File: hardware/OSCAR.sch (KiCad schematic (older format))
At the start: 0 parts

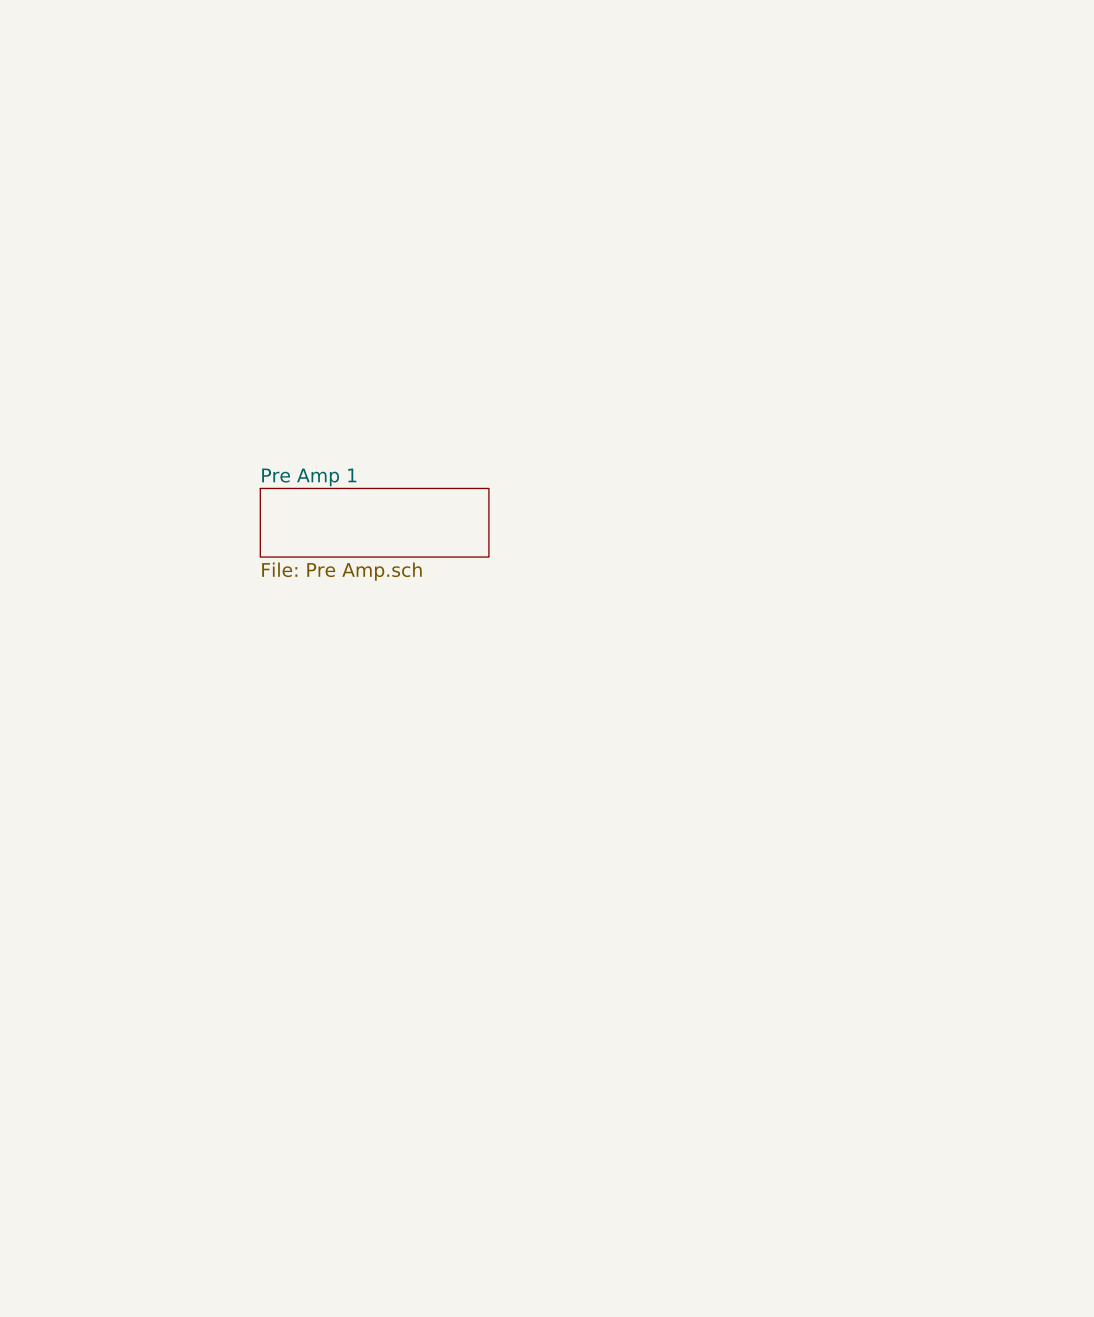
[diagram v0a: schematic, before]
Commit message: Added PCM 4204 and wired to pre amps
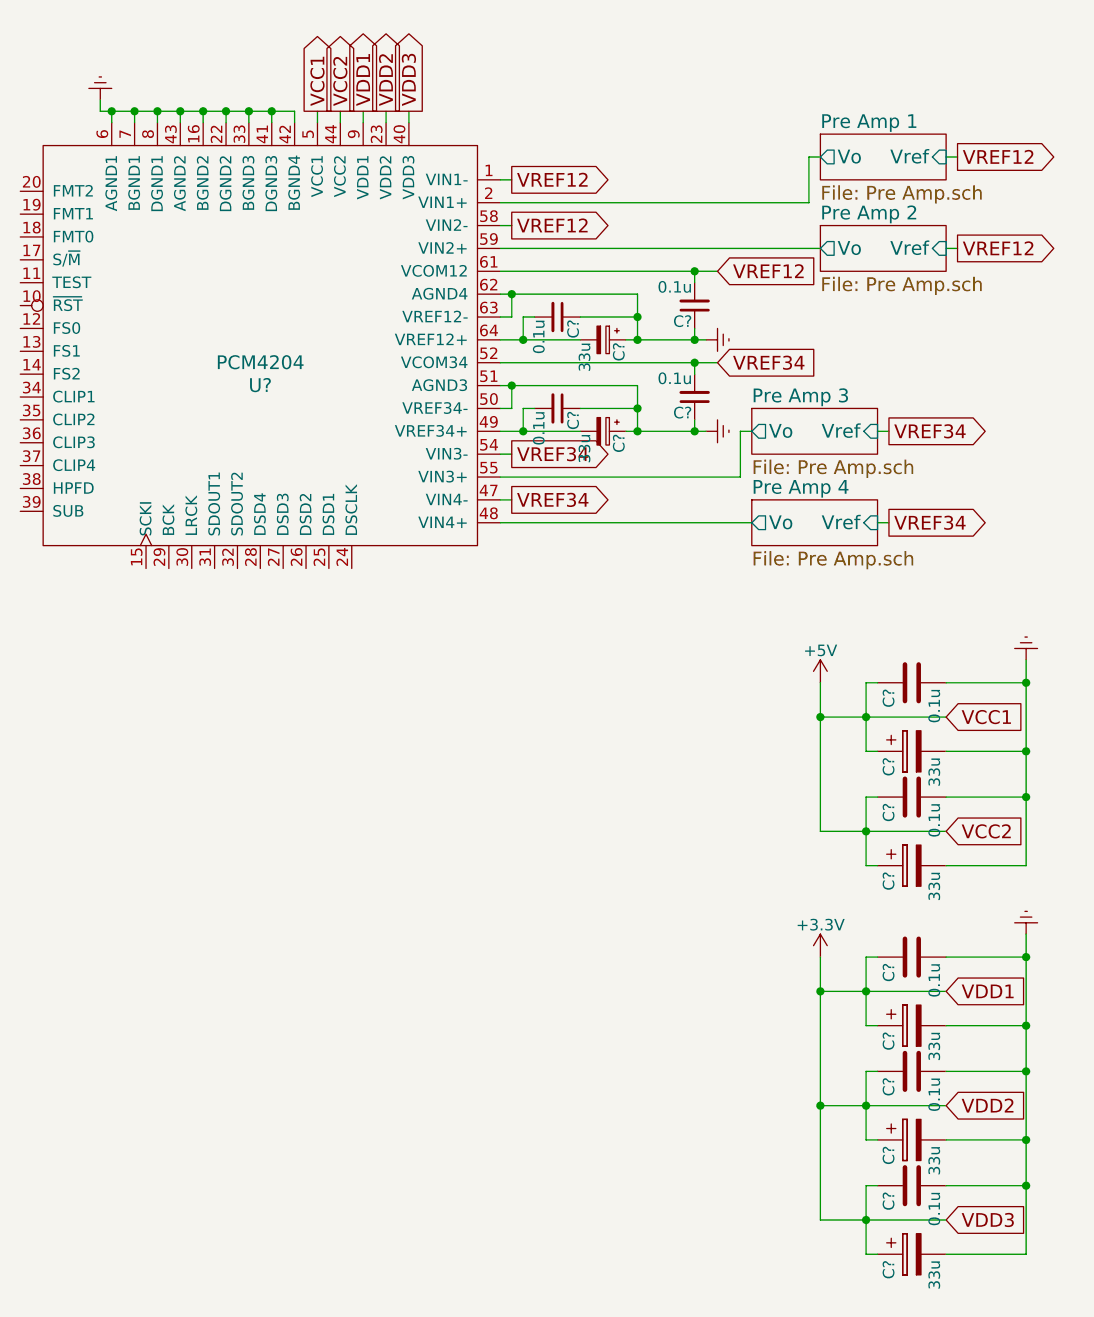
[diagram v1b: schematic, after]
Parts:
- added C? (x5): 0.1u, symbol C
- added C? (x5): 33u, symbol CP
- added C? (x4): 0.1u, symbol C_Small
- added C? (x2): 33u, symbol CP_Small
- added U?: PCM4204, symbol PCM4204
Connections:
- new net: C?.2, C?.2, U?.49 (VREF34+)
- new net: C?.2, C?.2, U?.64 (VREF12+)
- new net +3V3: C?.1, C?.1, C?.1, C?.1, C?.1, C?.1, U?.23 (VDD2), U?.40 (VDD3), U?.9 (VDD1)
- new net +5V: C?.1, C?.1, C?.1, C?.1, U?.44 (VCC2), U?.5 (VCC1)
- new net Earth: C?.1, C?.1, C?.1, C?.1, C?.1, C?.1, C?.2, C?.2, C?.2, C?.2, C?.2, C?.2, C?.2, C?.2, C?.2, C?.2, U?.16 (BGND2), U?.22 (DGND2), U?.33 (BGND3), U?.41 (DGND3), U?.42 (BGND4), U?.43 (AGND2), U?.50 (VREF34-), U?.51 (AGND3), U?.6 (AGND1), U?.62 (AGND4), U?.63 (VREF12-), U?.7 (BGND1), U?.8 (DGND1)
- new net Pre Amp 1/Vo: U?.2 (VIN1+)
- new net Pre Amp 2/Vo: U?.59 (VIN2+)
- new net Pre Amp 3/Vo: U?.55 (VIN3+)
- new net Pre Amp 4/Vo: U?.48 (VIN4+)
- new net VREF12: C?.2, U?.1 (VIN1-), U?.58 (VIN2-), U?.61 (VCOM12)
- new net VREF34: C?.2, U?.47 (VIN4-), U?.52 (VCOM34), U?.54 (VIN3-)

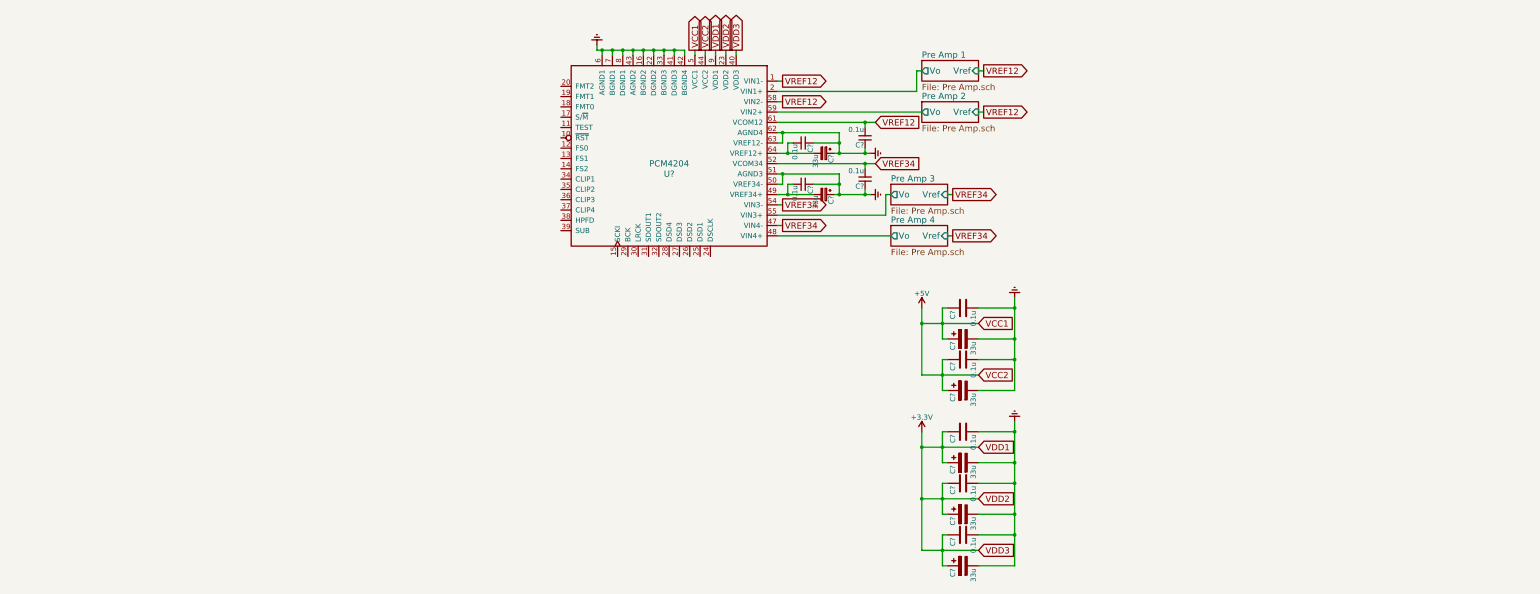
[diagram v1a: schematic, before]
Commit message: Add STM32 to Schematic
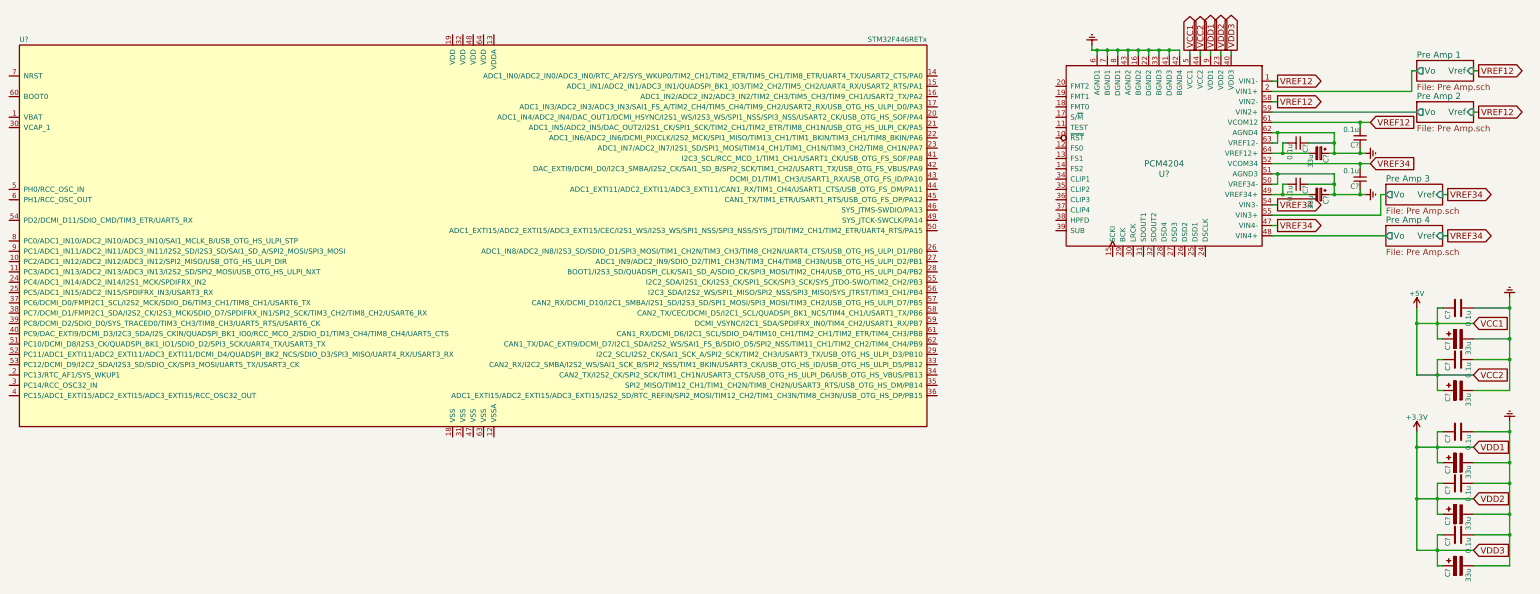
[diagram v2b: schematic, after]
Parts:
- added U?: STM32F446RETx, LQFP64, symbol STM32F446RETx
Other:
- moved on the sheet: C?, U?

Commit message: Added I2S connections and pin flags
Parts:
- added J?: USB_B, symbol USB_B
- added R? (x5): 100, symbol R
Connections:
- net +5V: now also J?.1 (VBUS)
- net Earth: now also U?.11 (TEST), J?.4 (GND), J?.5 (Shield)
- net RST: now reaches U?.10 (~RST)
- net FS0: now reaches U?.12 (FS0)
- net FS1: now reaches U?.13 (FS1)
- net FS2: now reaches U?.14 (FS2)
- net at U?.15 (SCKI): now also R?.1
- net S/~M: now reaches U?.17 (S/~M)
- net FMT0: now reaches U?.18 (FMT0)
- net FMT1: now reaches U?.19 (FMT1)
- net FMT2: now reaches U?.20 (FMT2)
- net at U?.29 (BCK): now also R?.1
- net at U?.30 (LRCK): now also R?.1
- net at U?.31 (SDOUT1): now also R?.1
- net at U?.32 (SDOUT2): now also R?.1
- net CLIP1: now reaches U?.34 (CLIP1)
- net CLIP2: now reaches U?.35 (CLIP2)
- net CLIP3: now reaches U?.36 (CLIP3)
- net CLIP4: now reaches U?.37 (CLIP4)
- net HPDF: now reaches U?.38 (HPFD)
- net SUB: now reaches U?.39 (SUB)
- net SCKI: now reaches U?.24 (PC4/ADC1_IN14/ADC2_IN14/I2S1_MCK/SPDIFRX_IN2)
- net SCKI: now also R?.2
- net BCK: now reaches U?.34 (CAN2_TX/I2S2_CK/SPI2_SCK/TIM1_CH1N/USART3_CTS/USB_OTG_HS_ULPI_D6/USB_OTG_HS_VBUS/PB13)
- net BCK: now also U?.55 (I2C2_SDA/I2S1_CK/I2S3_CK/SPI1_SCK/SPI3_SCK/SYS_JTDO-SWO/TIM2_CH2/PB3), R?.2
- net SD2: now reaches U?.36 (ADC1_EXTI15/ADC2_EXTI15/ADC3_EXTI15/I2S2_SD/RTC_REFIN/SPI2_MOSI/TIM12_CH2/TIM1_CH3N/TIM8_CH3N/USB_OTG_HS_DP/PB15)
- net SD2: now also R?.2
- net LRCK: now reaches U?.56 (I2C3_SDA/I2S2_WS/SPI1_MISO/SPI2_NSS/SPI3_MISO/SYS_JTRST/TIM3_CH1/PB4)
- net LRCK: now also R?.2
- net SD1: now reaches U?.57 (CAN2_RX/DCMI_D10/I2C1_SMBA/I2S1_SD/I2S3_SD/SPI1_MOSI/SPI3_MOSI/TIM3_CH2/USB_OTG_HS_ULPI_D7/PB5)
- net SD1: now also R?.2
- no-connect marks 0 -> 5
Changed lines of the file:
@@
 $EndComp
 $Comp
-L Earth #PWR?
+L Earth #PWR01
 U 1 1 595B8693
 P 11800 800
-F 0 "#PWR?" H 11800 550 50  0001 C CNN
+F 0 "#PWR01" H 11800 550 50  0001 C CNN
 F 1 "Earth" H 11800 650 50  0001 C CNN
 F 2 "" H 11800 800 50  0001 C CNN
@@
 VDD3
 $Comp
-L +5V #PWR?
+L +5V #PWR02
 U 1 1 595B9388
 P 14950 3350
-F 0 "#PWR?" H 14950 3200 50  0001 C CNN
+F 0 "#PWR02" H 14950 3200 50  0001 C CNN
 F 1 "+5V" H 14950 3490 50  0000 C CNN
 F 2 "" H 14950 3350 50  0001 C CNN
@@
 $EndComp
 $Comp
-L Earth #PWR?
+L Earth #PWR03
 U 1 1 595B9522
 P 15850 3250
-F 0 "#PWR?" H 15850 3000 50  0001 C CNN
+F 0 "#PWR03" H 15850 3000 50  0001 C CNN
 F 1 "Earth" H 15850 3100 50  0001 C CNN
 F 2 "" H 15850 3250 50  0001 C CNN
@@
 $EndComp
 $Comp
-L Earth #PWR?
+L Earth #PWR04
 U 1 1 595B9A44
 P 15850 4450
-F 0 "#PWR?" H 15850 4200 50  0001 C CNN
+F 0 "#PWR04" H 15850 4200 50  0001 C CNN
 F 1 "Earth" H 15850 4300 50  0001 C CNN
 F 2 "" H 15850 4450 50  0001 C CNN
@@
 Connection ~ 15850 3850
 $Comp
-L +3.3V #PWR?
+L +3.3V #PWR05
 U 1 1 595B9EEC
 P 14950 4550
-F 0 "#PWR?" H 14950 4400 50  0001 C CNN
+F 0 "#PWR05" H 14950 4400 50  0001 C CNN
 F 1 "+3.3V" H 14950 4690 50  0000 C CNN
 F 2 "" H 14950 4550 50  0001 C CNN
@@
 Connection ~ 13650 1850
 $Comp
-L Earth #PWR?
+L Earth #PWR06
 U 1 1 595BB36D
 P 14450 1850
-F 0 "#PWR?" H 14450 1600 50  0001 C CNN
+F 0 "#PWR06" H 14450 1600 50  0001 C CNN
 F 1 "Earth" H 14450 1700 50  0001 C CNN
 F 2 "" H 14450 1850 50  0001 C CNN
@@
 Connection ~ 13650 2250
 $Comp
-L Earth #PWR?
+L Earth #PWR07
 U 1 1 595BBE98
 P 14450 2250
-F 0 "#PWR?" H 14450 2000 50  0001 C CNN
+F 0 "#PWR07" H 14450 2000 50  0001 C CNN
 F 1 "Earth" H 14450 2100 50  0001 C CNN
 F 2 "" H 14450 2250 50  0001 C CNN
@@
 Text GLabel 13600 1350 2    60   Output ~ 0
 VREF12
-Text GLabel 13600 2350 2    60   Output ~ 0
+Text GLabel 14100 2350 2    60   Output ~ 0
 VREF34
 Text GLabel 13600 2550 2    60   Output ~ 0
@@
 	13550 1150 13600 1150
 Wire Wire Line
-	13550 2350 13600 2350
+	13550 2350 14100 2350
 Wire Wire Line
 	13550 2550 13600 2550
@@
 	1    0    0    -1
 $EndComp
+Text GLabel 12000 3150 3    60   Output ~ 0
+SCKI
+Text GLabel 12100 3150 3    60   BiDi ~ 0
+BCK
+Text GLabel 12200 3150 3    60   BiDi ~ 0
+LRCK
+Text GLabel 12300 3150 3    60   Input ~ 0
+SD1
+Text GLabel 12400 3150 3    60   Input ~ 0
+SD2
+$Comp
+L R R?
+U 1 1 595C4B9A
+P 12000 3000
+F 0 "R?" V 12080 3000 50  0000 C CNN
+F 1 "100" V 12000 3000 50  0000 C CNN
+F 2 "" V 11930 3000 50  0001 C CNN
+F 3 "" H 12000 3000 50  0001 C CNN
+	1    12000 3000
+	1    0    0    -1
+$EndComp
+$Comp
+L R R?
+U 1 1 595C4DB7
+P 12100 3000
+F 0 "R?" V 12180 3000 50  0000 C CNN
+F 1 "100" V 12100 3000 50  0000 C CNN
+F 2 "" V 12030 3000 50  0001 C CNN
+F 3 "" H 12100 3000 50  0001 C CNN
+	1    12100 3000
+	1    0    0    -1
+$EndComp
+$Comp
+L R R?
+U 1 1 595C4EC7
+P 12200 3000
+F 0 "R?" V 12280 3000 50  0000 C CNN
+F 1 "100" V 12200 3000 50  0000 C CNN
+F 2 "" V 12130 3000 50  0001 C CNN
+F 3 "" H 12200 3000 50  0001 C CNN
+	1    12200 3000
+	1    0    0    -1
+$EndComp
+$Comp
+L R R?
+U 1 1 595C4ECD
+P 12300 3000
+F 0 "R?" V 12380 3000 50  0000 C CNN
+F 1 "100" V 12300 3000 50  0000 C CNN
+F 2 "" V 12230 3000 50  0001 C CNN
+F 3 "" H 12300 3000 50  0001 C CNN
+	1    12300 3000
+	1    0    0    -1
+$EndComp
+$Comp
+L R R?
+U 1 1 595C4F19
+P 12400 3000
+F 0 "R?" V 12480 3000 50  0000 C CNN
+F 1 "100" V 12400 3000 50  0000 C CNN
+F 2 "" V 12330 3000 50  0001 C CNN
+F 3 "" H 12400 3000 50  0001 C CNN
+	1    12400 3000
+	1    0    0    -1
+$EndComp
+Text GLabel 10350 3100 2    60   BiDi ~ 0
+BCK
+Text GLabel 10350 3200 2    60   BiDi ~ 0
+LRCK
+Text GLabel 10350 3300 2    60   Output ~ 0
+SD1
+Text GLabel 10350 4200 2    60   Output ~ 0
+SD2
+Text GLabel 10350 4000 2    60   BiDi ~ 0
+BCK
+Wire Wire Line
+	10300 3100 10350 3100
+Wire Wire Line
+	10300 3200 10350 3200
+Wire Wire Line
+	10300 3300 10350 3300
+Wire Wire Line
+	10300 4000 10350 4000
+Wire Wire Line
+	10300 4200 10350 4200
+Text GLabel 1250 3100 0    60   Input ~ 0
+SCKI
+Wire Wire Line
+	1250 3100 1300 3100
+$Comp
+L USB_B J?
+U 1 1 595C8EF7
+P 1700 9700
+F 0 "J?" H 1500 10150 50  0000 L CNN
+F 1 "USB_B" H 1500 10050 50  0000 L CNN
+F 2 "" H 1850 9650 50  0001 C CNN
+F 3 "" H 1850 9650 50  0001 C CNN
+	1    1700 9700
+	1    0    0    -1
+$EndComp
+$Comp
+L +5V #PWR08
+U 1 1 595C96F2
+P 2050 9500
+F 0 "#PWR08" H 2050 9350 50  0001 C CNN
+F 1 "+5V" H 2050 9640 50  0000 C CNN
+F 2 "" H 2050 9500 50  0001 C CNN
+F 3 "" H 2050 9500 50  0001 C CNN
+	1    2050 9500
+	0    1    1    0
+$EndComp
+$Comp
+L Earth #PWR09
+U 1 1 595CA426
+P 1700 10200
+F 0 "#PWR09" H 1700 9950 50  0001 C CNN
+F 1 "Earth" H 1700 10050 50  0001 C CNN
+F 2 "" H 1700 10200 50  0001 C CNN
+F 3 "" H 1700 10200 50  0001 C CNN
+	1    1700 10200
+	1    0    0    -1
+$EndComp
+Wire Wire Line
+	1600 10100 1600 10150
+Wire Wire Line
+	1600 10150 1700 10150
+Wire Wire Line
+	1700 10100 1700 10200
+Connection ~ 1700 10150
+Wire Wire Line
+	2000 9500 2050 9500
+NoConn ~ 12500 2850
+NoConn ~ 12600 2850
+NoConn ~ 12700 2850
+NoConn ~ 12800 2850
+NoConn ~ 12900 2850
+Text GLabel 11400 1200 0    60   Output ~ 0
+FMT2
+Text GLabel 11400 1300 0    60   Output ~ 0
+FMT1
+Text GLabel 11400 1400 0    60   Output ~ 0
+FMT0
+Text GLabel 11400 1500 0    60   Output ~ 0
+S/~M
+Text GLabel 11400 1700 0    60   Output ~ 0
+RST
+Text GLabel 11400 1800 0    60   Output ~ 0
+FS0
+Text GLabel 11400 1900 0    60   Output ~ 0
+FS1
+Text GLabel 11400 2000 0    60   Output ~ 0
+FS2
+Text GLabel 11400 2100 0    60   Output ~ 0
+CLIP1
+Text GLabel 11400 2200 0    60   Output ~ 0
+CLIP2
+Text GLabel 11400 2300 0    60   Output ~ 0
+CLIP3
+Text GLabel 11400 2400 0    60   Output ~ 0
+CLIP4
+Text GLabel 11400 2500 0    60   Input ~ 0
+HPDF
+Text GLabel 11400 2600 0    60   Input ~ 0
+SUB
+$Comp
+L Earth #PWR010
+U 1 1 595CBD08
+P 11100 1650
+F 0 "#PWR010" H 11100 1400 50  0001 C CNN
+F 1 "Earth" H 11100 1500 50  0001 C CNN
+F 2 "" H 11100 1650 50  0001 C CNN
+F 3 "" H 11100 1650 50  0001 C CNN
+	1    11100 1650
+	1    0    0    -1
+$EndComp
+Wire Wire Line
+	11450 1600 11100 1600
+Wire Wire Line
+	11100 1600 11100 1650
+Wire Wire Line
+	11400 1700 11450 1700
+Wire Wire Line
+	11400 1800 11450 1800
+Wire Wire Line
+	11400 1900 11450 1900
+Wire Wire Line
+	11400 2000 11450 2000
+Wire Wire Line
+	11400 2100 11450 2100
+Wire Wire Line
+	11400 2200 11450 2200
+Wire Wire Line
+	11400 2300 11450 2300
+Wire Wire Line
+	11400 2400 11450 2400
+Wire Wire Line
+	11400 2500 11450 2500
+Wire Wire Line
+	11400 2600 11450 2600
+Wire Wire Line
+	11400 1200 11450 1200
+Wire Wire Line
+	11400 1300 11450 1300
+Wire Wire Line
+	11400 1400 11450 1400
+Wire Wire Line
+	11400 1500 11450 1500
 $EndSCHEMATC
